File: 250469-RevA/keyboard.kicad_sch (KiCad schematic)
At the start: 9 parts, among them J1 Conn_01x20_Pin, U1 6526A, U23 74LS14

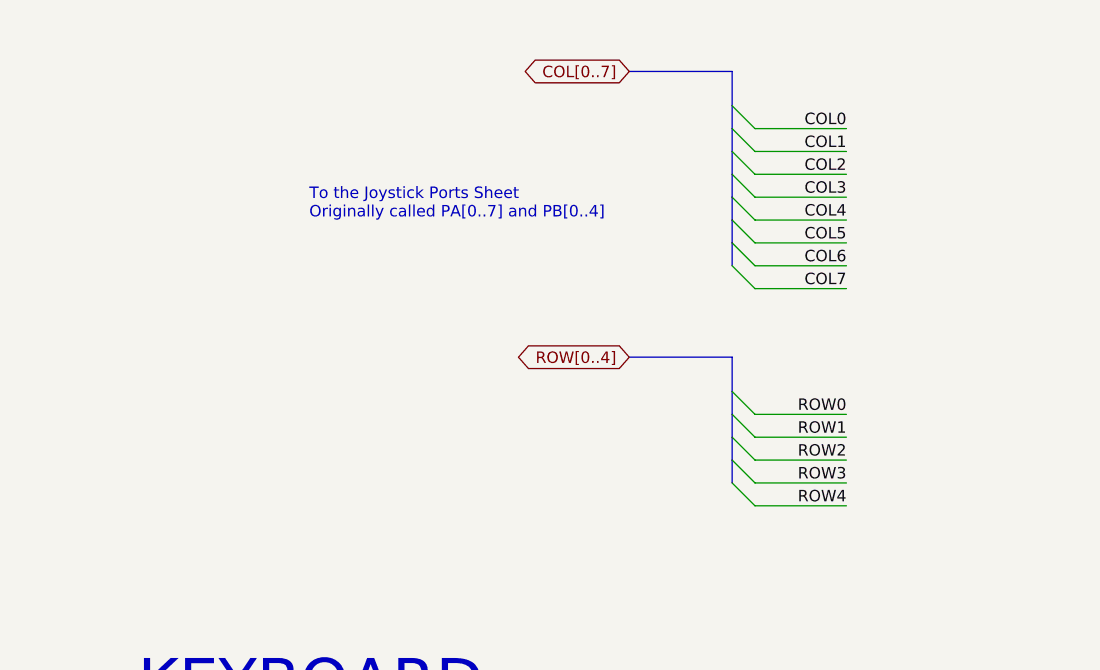
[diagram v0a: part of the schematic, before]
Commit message: Footprints and Symbols updates
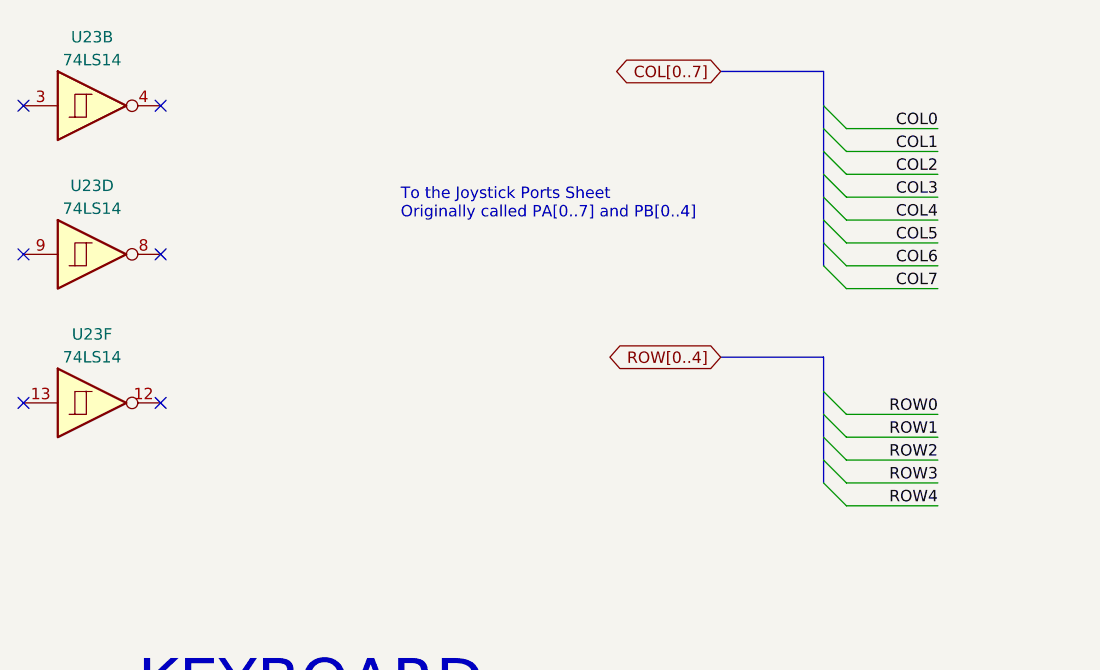
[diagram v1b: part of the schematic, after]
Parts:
- added unit 6 of U23
- added unit 2 of U23
- added unit 4 of U23
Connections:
- no-connect marks 2 -> 8

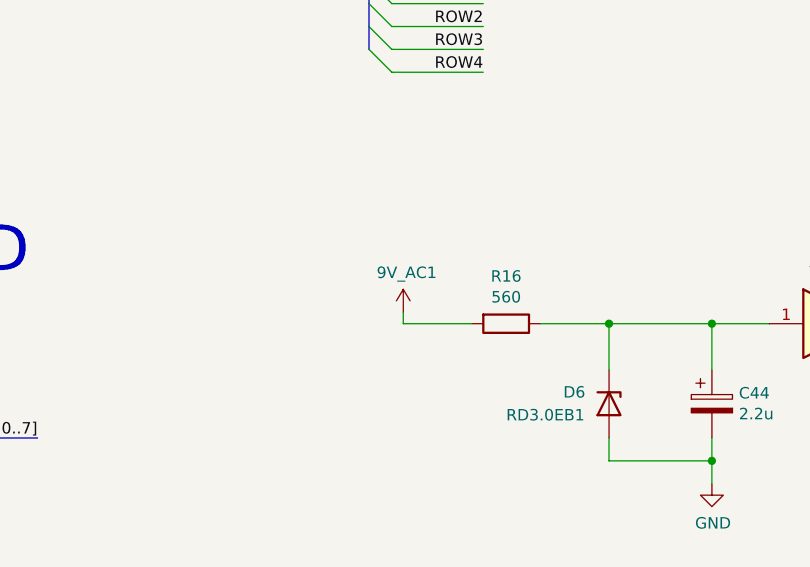
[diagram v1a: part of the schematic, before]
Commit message: Fixes after renaming the project library
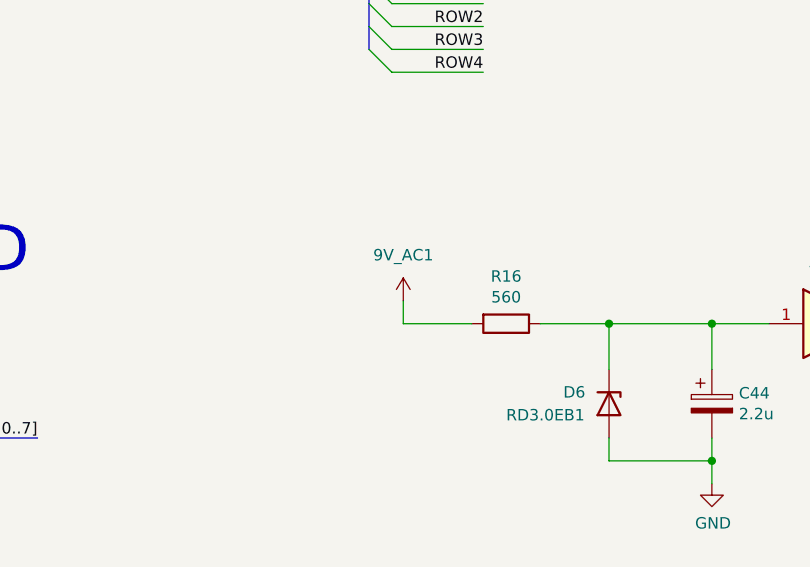
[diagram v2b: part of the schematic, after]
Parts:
- L4: footprint 250469-01:L_Radial_L7.5mm_W3mm_P5.00mm_Kemet_SBT-02 -> C64-C-250469:L_Radial_L7.5mm_W3mm_P5.00mm_Kemet_SBT-02
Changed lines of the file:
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@@
     (stroke (width 0) (type default))
   )
-  (wire (pts (xy 116.84 101.6) (xy 116.84 100.33))
+  (wire (pts (xy 116.84 101.6) (xy 116.84 99.06))
     (stroke (width 0) (type default))
   )
@@
       (effects (font (size 1.27 1.27)))
     )
-    (property "Footprint" "250469-01:L_Radial_L7.5mm_W3mm_P5.00mm_Kemet_SBT-02" (at 71.12 163.83 0)
+    (property "Footprint" "C64-C-250469:L_Radial_L7.5mm_W3mm_P5.00mm_Kemet_SBT-02" (at 71.12 163.83 0)
       (effects (font (size 1.27 1.27)) hide)
     )
@@
         (path "/ceb6c8ef-b249-4909-95e5-e7359667aee8/00000000-0000-0000-0000-00005e4c440a"
           (reference "#PWR0116") (unit 1)
-        )
-      )
-    )
-  )
-  (symbol (lib_id "250469-01:9V_AC1") (at 116.84 100.33 0) (unit 1)
-    (in_bom yes) (on_board yes) (dnp no)
-    (property "Reference" "#PWR02" (at 116.84 104.14 0)
-      (effects (font (size 1.27 1.27)) hide)
-    )
-    (property "Value" "9V_AC1" (at 117.221 95.9358 0)
-      (effects (font (size 1.27 1.27)))
-    )
-    (property "Footprint" "" (at 116.84 100.33 0)
-      (effects (font (size 1.27 1.27)) hide)
-    )
-    (property "Datasheet" "" (at 116.84 100.33 0)
-      (effects (font (size 1.27 1.27)) hide)
-    )
-    (pin "1")
-    (instances
-      (project "C64C-250469-01-A"
-        (path "/ceb6c8ef-b249-4909-95e5-e7359667aee8/00000000-0000-0000-0000-00005e4c440a"
-          (reference "#PWR02") (unit 1)
         )
       )
@@
         )
       )
+    )
+  )
+  (symbol (lib_id "C64-C-250469:9V_AC1") (at 116.84 99.06 0) (unit 1)
+    (in_bom yes) (on_board yes) (dnp no) (fields_autoplaced)
+    (property "Reference" "#PWR02" (at 116.84 102.87 0)
+      (effects (font (size 1.27 1.27)) hide)
+    )
+    (property "Value" "9V_AC1" (at 116.84 93.98 0)
+      (effects (font (size 1.27 1.27)))
+    )
+    (property "Footprint" "" (at 116.84 99.06 0)
+      (effects (font (size 1.27 1.27)) hide)
+    )
+    (property "Datasheet" "" (at 116.84 99.06 0)
+      (effects (font (size 1.27 1.27)) hide)
+    )
+    (pin "1")
+    (instances
+      (project "C64C-250469-01-A"
+        (path "/ceb6c8ef-b249-4909-95e5-e7359667aee8/00000000-0000-0000-0000-00005e4c440a"
+          (reference "#PWR02") (unit 1)
+        )
+      )
